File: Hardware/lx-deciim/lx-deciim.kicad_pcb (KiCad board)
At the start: 2 copper layers, 64.1 x 108 mm, 147 parts, among them IC1 AZ1117CH2-5.0TRG1, J1 AudioJack2_SwitchT, J10 AudioJack2_SwitchT, J11 AudioJack2_SwitchT, J12 AudioJack2_SwitchT, J13 AudioJack2_SwitchT, J14 AudioJack2_SwitchT, J15 AudioJack2_SwitchT, J16 AudioJack2_SwitchT, J17 Conn_01x10, J18 Conn_01x15_Pin, J19 Conn_01x15_Socket, J2 AudioJack2_SwitchT, J20 Conn_01x15_Pin, J21 Conn_01x15_Socket, J3 AudioJack2_SwitchT, J4 AudioJack2_SwitchT, J5 AudioJack2_SwitchT, J6 AudioJack2_SwitchT, J7 AudioJack2_SwitchT, J8 AudioJack2_SwitchT, J9 AudioJack2_SwitchT, U1 MCP6004, U2 MCP6001-OT, U3 MCP6004, U4 MCP6004, U5 TL074, U6 MCP6004

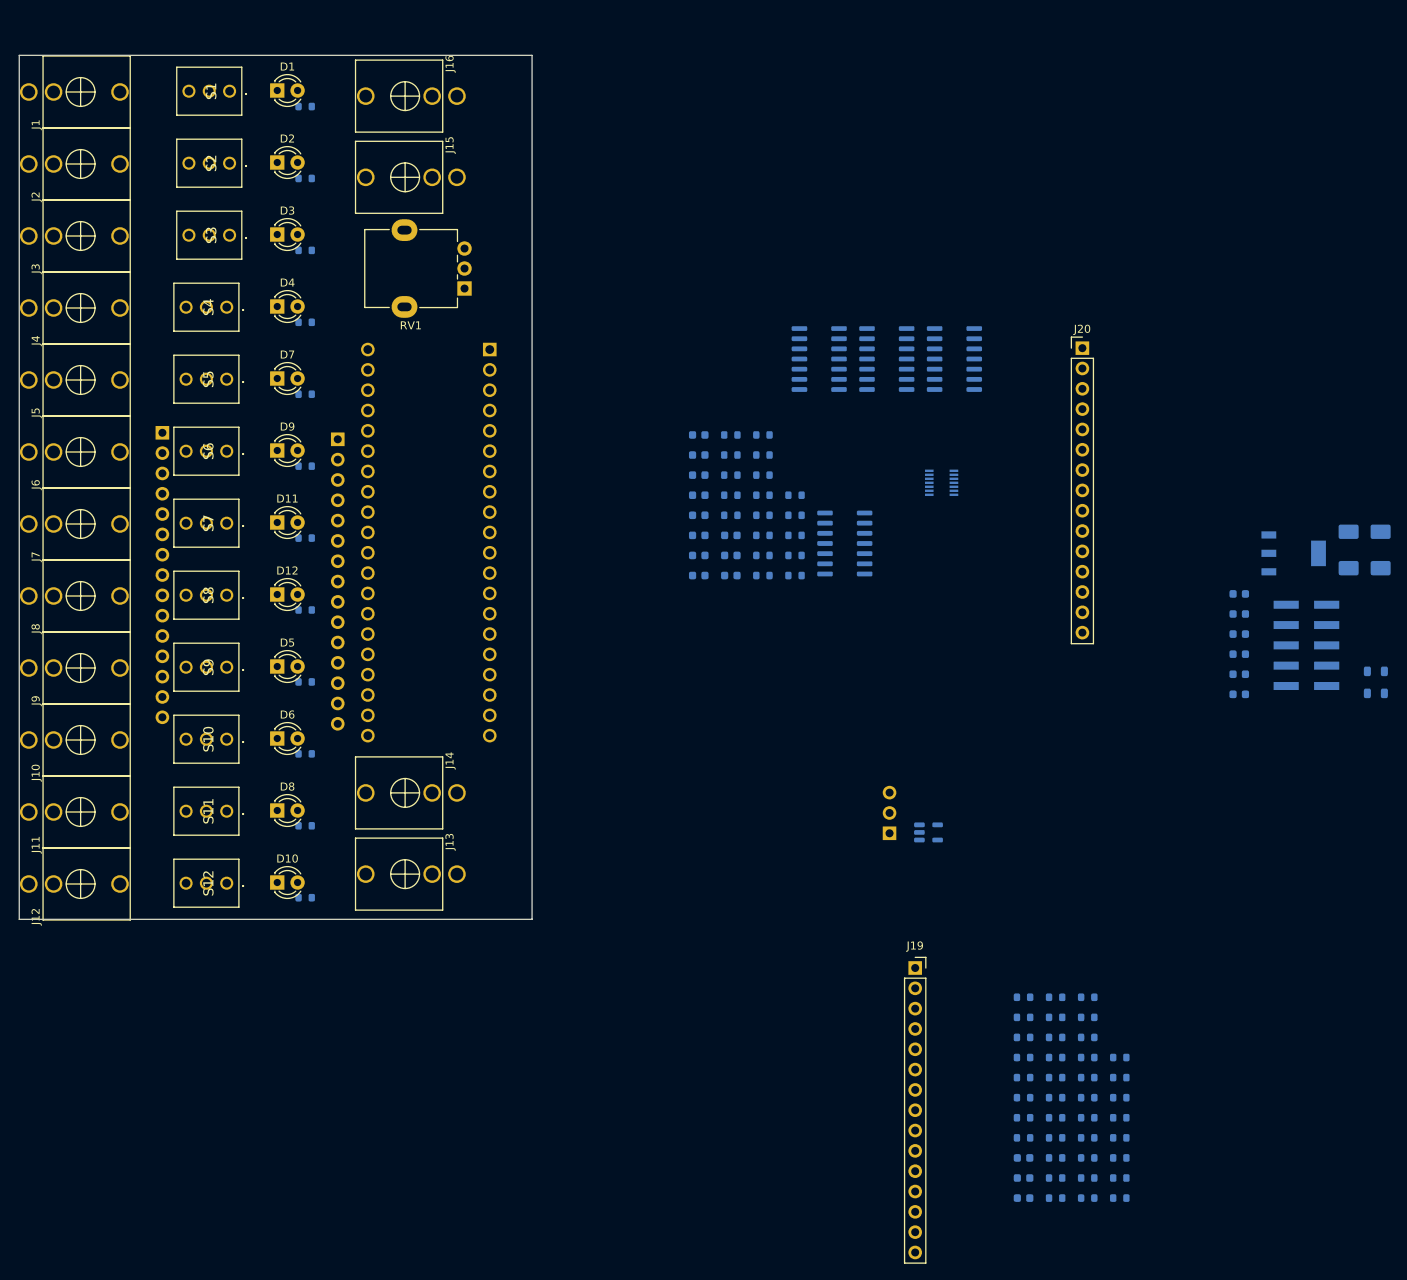
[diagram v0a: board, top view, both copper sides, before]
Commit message: feature: first draft routing
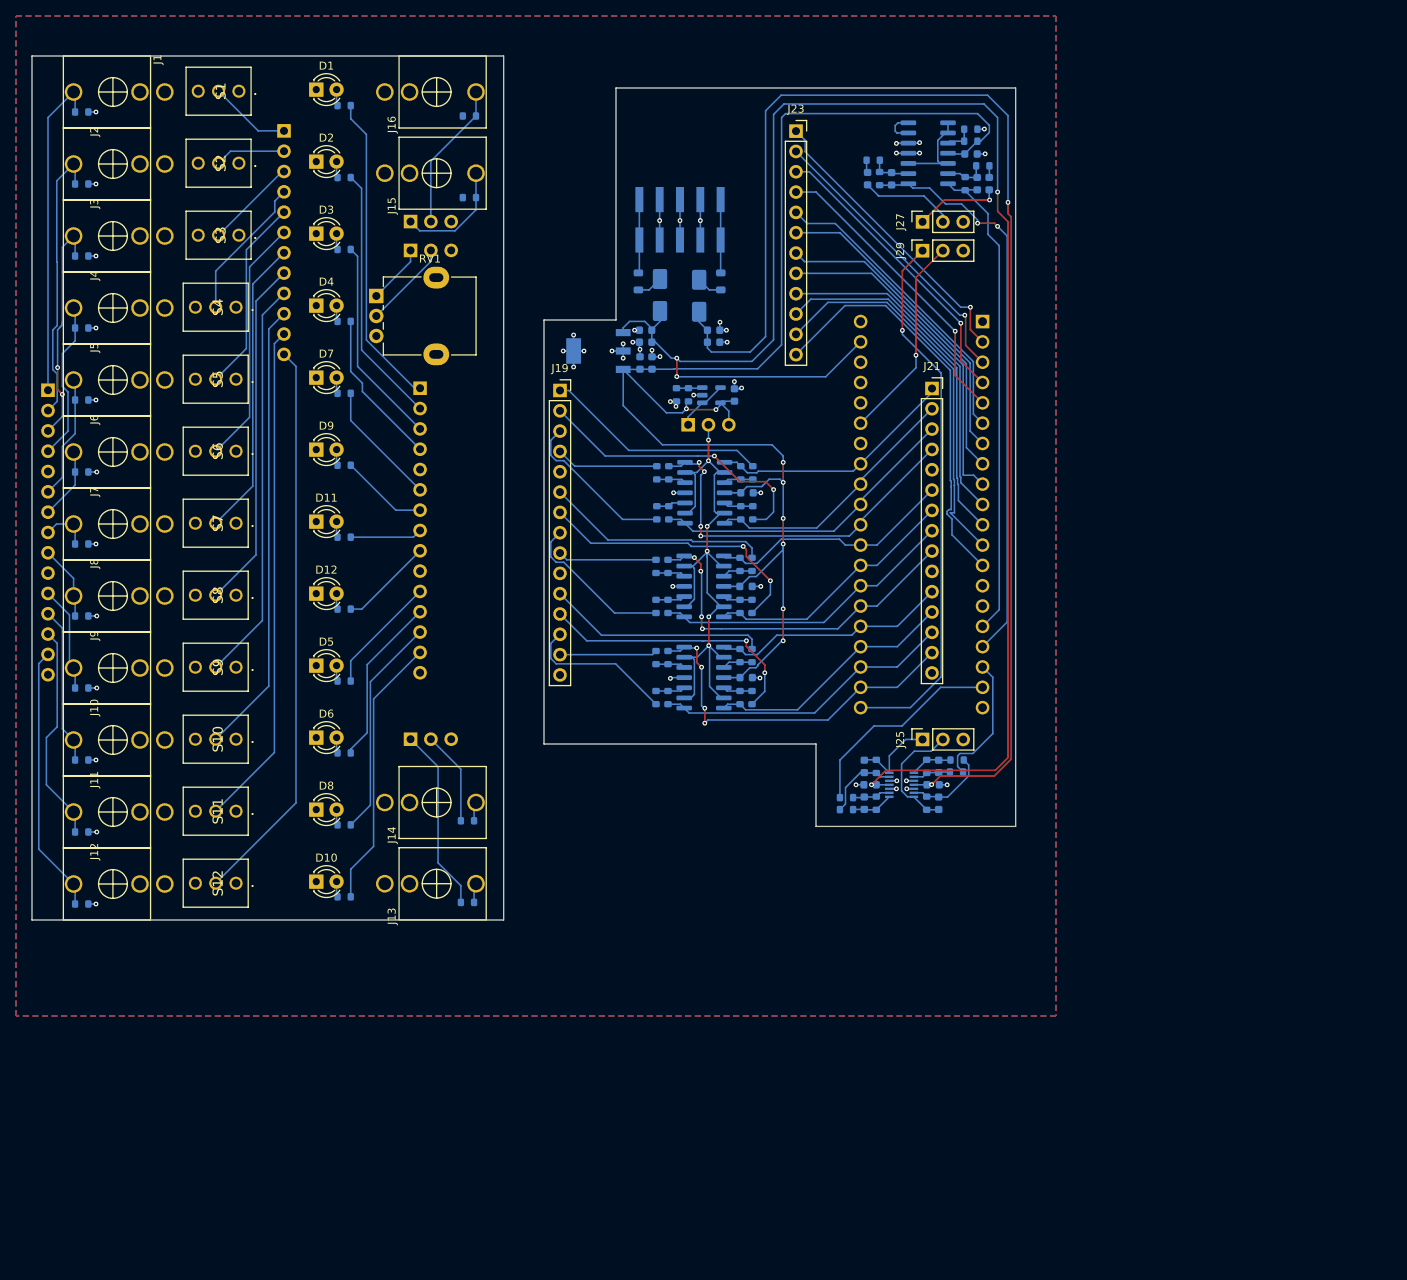
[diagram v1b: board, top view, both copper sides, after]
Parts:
- added C21: 100n, Capacitor_SMD:C_0603_1608Metric, B.Cu at (114.8, 72.4)
- added J22: Conn_01x12_Pin, Connector_PinHeader_2.54mm:PinHeader_1x12_P2.54mm_Vertical, B.Cu at (58.5, 39.4)
- added J23: Conn_01x12_Socket, Connector_PinSocket_2.54mm:PinSocket_1x12_P2.54mm_Vertical, F.Cu at (122.5, 39.4)
- added J24: Conn_01x03_Pin, Connector_PinHeader_2.54mm:PinHeader_1x03_P2.54mm_Vertical, B.Cu at (74.3, 115.4)
- added J25: Conn_01x03_Socket, Connector_PinSocket_2.54mm:PinSocket_1x03_P2.54mm_Vertical, F.Cu at (138.3, 115.4)
- added J26: Conn_01x03_Pin, Connector_PinHeader_2.54mm:PinHeader_1x03_P2.54mm_Vertical, B.Cu at (74.3, 50.7)
- added J27: Conn_01x03_Socket, Connector_PinSocket_2.54mm:PinSocket_1x03_P2.54mm_Vertical, F.Cu at (138.3, 50.7)
- added J28: Conn_01x03_Pin, Connector_PinHeader_2.54mm:PinHeader_1x03_P2.54mm_Vertical, B.Cu at (74.3, 54.3)
- added J29: Conn_01x03_Socket, Connector_PinSocket_2.54mm:PinSocket_1x03_P2.54mm_Vertical, F.Cu at (138.3, 54.3)
- J20: moved to B.Cu
- J21: moved to F.Cu
- moved R13 169.4 mm to (33.2, 55.0)
- moved R3 168.6 mm to (33.2, 37.0)
- moved R19 161.6 mm to (33.2, 64.0)
- moved R9 158.9 mm to (33.2, 46.0)
- moved R30 148.3 mm to (33.2, 73.0)
- moved R38 142.0 mm to (33.2, 82.0)
- moved R45 136.5 mm to (33.2, 91.0)
- moved R21 134.0 mm to (33.2, 109.0)
- moved R49 131.7 mm to (33.2, 100.0)
- moved R26 130.4 mm to (33.2, 118.0)
- moved R34 127.9 mm to (33.2, 127.0)
- moved R42 126.3 mm to (33.2, 136.0)
- moved FB1 105.6 mm to (102.8, 58.2), turned to -90 degrees
- moved R5 101.9 mm to (109.1, 72.3), turned to -90 degrees
- moved R7 100.2 mm to (107.6, 72.3), turned to 90 degrees
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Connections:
- A1 pad 10: /switches/sw_08 -> Net-(A1-SPI1_POCI)
- A1 pad 11: /switches/sw_09 -> Net-(A1-SPI1_PICO)
- A1 pad 12: /switches/sw_10 -> Net-(A1-I2C1_SCL)
- A1 pad 13: /switches/sw_11 -> Net-(A1-I2C1_SDA)
- A1 pad 2: /switches/sw_00 -> Net-(A1-SD_DATA_3)
- A1 pad 22: /triggers/trig_sig_00 -> trig_sig'_11
- A1 pad 23: /triggers/trig_sig_01 -> trig_sig'_10
- A1 pad 24: /triggers/trig_sig_02 -> trig_sig'_09
- A1 pad 25: /triggers/trig_sig_03 -> trig_sig'_08
- A1 pad 26: /triggers/trig_sig_04 -> trig_sig'_07
- A1 pad 27: /triggers/trig_sig_05 -> trig_sig'_06
- A1 pad 28: /triggers/trig_sig_06 -> trig_sig'_05
- A1 pad 29: /triggers/trig_sig_07 -> trig_sig'_04
- A1 pad 3: /switches/sw_01 -> Net-(A1-SD_DATA_2)
- A1 pad 30: /triggers/trig_sig_08 -> trig_sig'_03
- A1 pad 31: /triggers/trig_sig_09 -> trig_sig'_02
- A1 pad 32: /triggers/trig_sig_10 -> trig_sig'_01
- A1 pad 33: /triggers/trig_sig_11 -> trig_sig'_00
- A1 pad 4: /switches/sw_02 -> Net-(A1-SD_DATA_1)
- A1 pad 5: /switches/sw_03 -> Net-(A1-SD_DATA_0)
- A1 pad 6: /switches/sw_04 -> Net-(A1-SD_CMD)
- A1 pad 7: /switches/sw_05 -> Net-(A1-SD_CLK)
- A1 pad 8: /switches/sw_06 -> Net-(A1-SPI1_CS)
- A1 pad 9: /switches/sw_07 -> Net-(A1-SPI1_SCK)
- C11 pad 1: Net-(C11-Pad1) -> In'_R
- C14 pad 1: Net-(C14-Pad1) -> In'_L
- C5 pad 2: Net-(C5-Pad2) -> Out'_R
- C9 pad 2: Net-(C9-Pad2) -> Out'_L
- J15 pad T: Net-(C11-Pad1) -> In_R
- J16 pad T: Net-(C14-Pad1) -> In_L
- J20 pad 1: trig_sig'_00 -> trig_sig_00
- J20 pad 11: trig_sig'_08 -> trig_sig_08
- J20 pad 12: trig_sig'_09 -> trig_sig_09
- J20 pad 13: trig_sig'_10 -> trig_sig_10
- J20 pad 14: trig_sig'_11 -> trig_sig_11
- J20 pad 2: trig_sig'_01 -> trig_sig_01
- J20 pad 3: trig_sig'_02 -> trig_sig_02
- J20 pad 4: trig_sig'_03 -> trig_sig_03
- J20 pad 6: trig_sig'_04 -> trig_sig_04
- J20 pad 7: trig_sig'_05 -> trig_sig_05
- J20 pad 8: trig_sig'_06 -> trig_sig_06
- J20 pad 9: trig_sig'_07 -> trig_sig_07
- J21 pad 1: /triggers/trig_sig_00 -> trig_sig'_00
- J21 pad 11: /triggers/trig_sig_08 -> trig_sig'_08
- J21 pad 12: /triggers/trig_sig_09 -> trig_sig'_09
- J21 pad 13: /triggers/trig_sig_10 -> trig_sig'_10
- J21 pad 14: /triggers/trig_sig_11 -> trig_sig'_11
- J21 pad 2: /triggers/trig_sig_01 -> trig_sig'_01
- J21 pad 3: /triggers/trig_sig_02 -> trig_sig'_02
- J21 pad 4: /triggers/trig_sig_03 -> trig_sig'_03
- J21 pad 6: /triggers/trig_sig_04 -> trig_sig'_04
- J21 pad 7: /triggers/trig_sig_05 -> trig_sig'_05
- J21 pad 8: /triggers/trig_sig_06 -> trig_sig'_06
- J21 pad 9: /triggers/trig_sig_07 -> trig_sig'_07
- R10 pad 1: /triggers/trig_sig_01 -> trig_sig_01
- R13 pad 1: I'_02 -> I_02
- R14 pad 1: /triggers/trig_sig_02 -> trig_sig_02
- R19 pad 1: I'_03 -> I_03
- R20 pad 1: /triggers/trig_sig_03 -> trig_sig_03
- R21 pad 1: I'_08 -> I_08
- R22 pad 1: /triggers/trig_sig_08 -> trig_sig_08
- R26 pad 1: I'_09 -> I_09
- R27 pad 1: /triggers/trig_sig_09 -> trig_sig_09
- R3 pad 1: I'_00 -> I_00
- R30 pad 1: I'_04 -> I_04
- R31 pad 1: /triggers/trig_sig_04 -> trig_sig_04
- R34 pad 1: I'_10 -> I_10
- R35 pad 1: /triggers/trig_sig_10 -> trig_sig_10
- R38 pad 1: I'_05 -> I_05
- R39 pad 1: /triggers/trig_sig_05 -> trig_sig_05
- R4 pad 1: /triggers/trig_sig_00 -> trig_sig_00
- R42 pad 1: I'_11 -> I_11
- R43 pad 1: /triggers/trig_sig_11 -> trig_sig_11
- R45 pad 1: I'_06 -> I_06
- R46 pad 1: /triggers/trig_sig_06 -> trig_sig_06
- R49 pad 1: I'_07 -> I_07
- R50 pad 1: /triggers/trig_sig_07 -> trig_sig_07
- R52 pad 2: Net-(C5-Pad2) -> Out'_R
- R55 pad 2: Net-(C5-Pad2) -> Out_R
- R57 pad 2: Net-(C9-Pad2) -> Out'_L
- R60 pad 2: Net-(C9-Pad2) -> Out_L
- R64 pad 1: Net-(C11-Pad1) -> In_R
- R68 pad 1: Net-(C14-Pad1) -> In_L
- R9 pad 1: I'_01 -> I_01
- RV1 pad 1: +3V3 -> Net-(J28-Pin_1)
- RV1 pad 2: Net-(A1-SAI2_SCK) -> Net-(J28-Pin_2)
- U5 pad 14: Net-(C9-Pad2) -> Out'_L
- U5 pad 7: Net-(C5-Pad2) -> Out'_R
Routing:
- net +12V: track 0.00 -> 212.5 mm, vias 0 -> 4
- net +5V: track 0.00 -> 182.6 mm, vias 0 -> 8
- net -12V: track 0.00 -> 167.7 mm, vias 0 -> 2
- net trigger_comp_level: track 0.00 -> 81.2 mm, vias 0 -> 6
- net /audio_io/audio_in_L_daisy_level: track 0.00 -> 71.6 mm, vias 0 -> 2
- net /switches/sw_11: track 0.00 -> 70.9 mm
- net GND: track 0.00 -> 70.1 mm, vias 0 -> 53
- net +3V3: track 0.00 -> 68.0 mm, vias 0 -> 1
- net /switches/sw_10: track 0.00 -> 63.2 mm
- net /audio_io/audio_in_R_daisy_level: track 0.00 -> 61.1 mm
- net /switches/sw_09: track 0.00 -> 56.7 mm
- net Net-(A1-I2C1_SDA): track 0.00 -> 51.8 mm
- net /switches/sw_08: track 0.00 -> 50.3 mm
- net Net-(A1-I2C1_SCL): track 0.00 -> 49.0 mm
- net trig_sig'_03: track 0.00 -> 47.5 mm, vias 0 -> 4
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- added copper zone on B.Cu, net GND
- added copper zone on F.Cu, net GND
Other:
- board size 64.1 x 108 mm -> 123 x 108 mm

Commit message: feature: clean routing
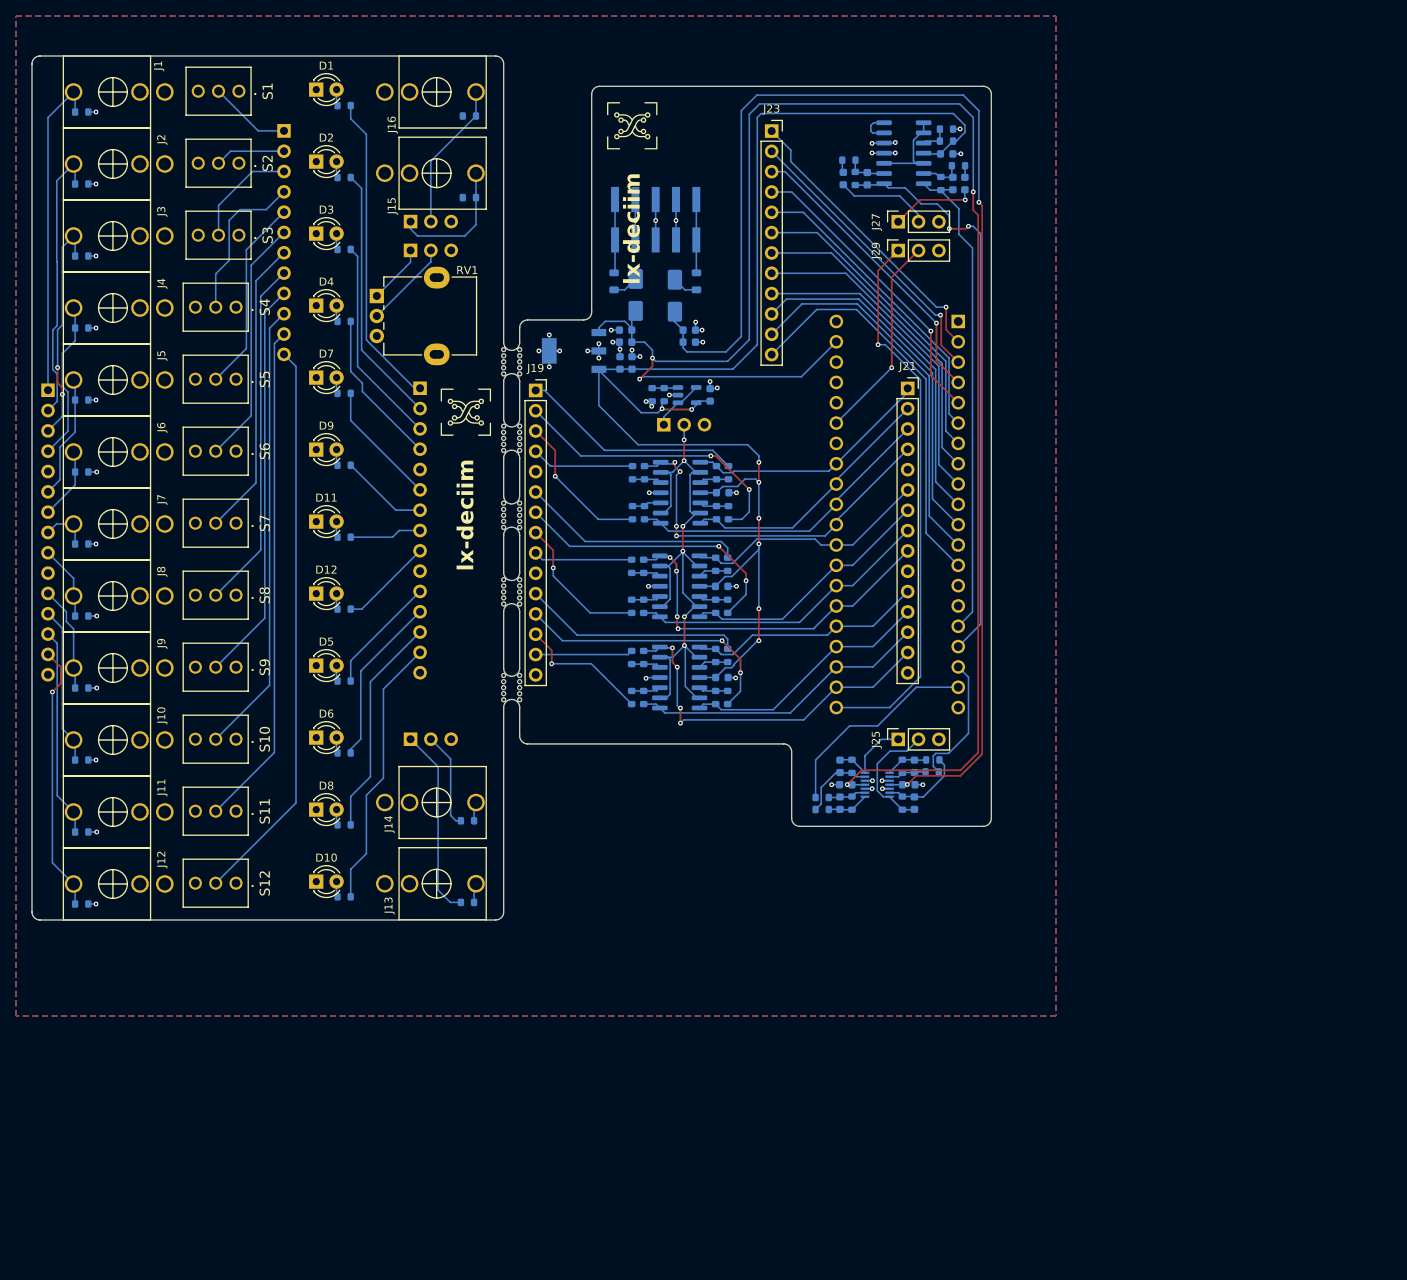
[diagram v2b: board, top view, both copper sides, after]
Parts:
- added ?: , , F.Cu at (88.0, 85.9)
- added ?: , , F.Cu at (86.0, 78.5)
- added ?: , , F.Cu at (88.0, 77.8)
- added ?: , , F.Cu at (86.0, 69.7)
- added ?: , , F.Cu at (86.0, 110.5)
- added ?: , , F.Cu at (88.0, 97.8)
- added ?: , , F.Cu at (88.0, 88.9)
- added ?: , , F.Cu at (86.0, 108.2)
- added ?: , , F.Cu at (88.0, 68.2)
- added ?: , , F.Cu at (88.0, 69.7)
- added ?: , , F.Cu at (88.0, 69.0)
- added ?: , , F.Cu at (88.0, 79.3)
- added ?: , , F.Cu at (86.0, 76.3)
- added ?: , , F.Cu at (88.0, 88.2)
- added ?: , , F.Cu at (88.0, 76.3)
- added ?: , , F.Cu at (88.0, 67.5)
- added ?: , , F.Cu at (86.0, 85.9)
- added ?: , , F.Cu at (88.0, 77.0)
- added ?: , , F.Cu at (86.0, 68.2)
- added ?: , , F.Cu at (86.0, 109.0)
- added ?: , , F.Cu at (88.0, 97.0)
- added ?: , , F.Cu at (86.0, 107.4)
- added ?: , , F.Cu at (88.0, 95.5)
- added ?: , , F.Cu at (86.0, 69.0)
- added ?: , , F.Cu at (88.0, 109.0)
- added ?: , , F.Cu at (86.0, 87.4)
- added ?: , , F.Cu at (88.0, 107.4)
- added ?: , , F.Cu at (88.0, 109.7)
- added ?: , , F.Cu at (88.0, 78.6)
- added ?: , , F.Cu at (86.0, 77.0)
- added ?: , , F.Cu at (86.0, 79.3)
- added ?: , , F.Cu at (86.0, 97.7)
- added ?: , , F.Cu at (88.0, 108.2)
- added ?: , , F.Cu at (86.0, 86.7)
- added ?: , , F.Cu at (86.0, 67.5)
- added ?: , , F.Cu at (88.0, 98.5)
- added ?: , , F.Cu at (86.0, 88.9)
- added ?: , , F.Cu at (86.0, 77.8)
- added ?: , , F.Cu at (88.0, 86.7)
- added ?: , , F.Cu at (86.0, 98.5)
- added ?: , , F.Cu at (88.0, 66.7)
- added ?: , , F.Cu at (86.0, 66.7)
- added ?: , , F.Cu at (86.0, 96.2)
- added ?: , , F.Cu at (88.0, 87.4)
- added ?: , , F.Cu at (88.0, 96.2)
- added ?: , , F.Cu at (86.0, 97.0)
- added ?: , , F.Cu at (86.0, 109.7)
- added ?: , , F.Cu at (88.0, 110.5)
- added ?: , , F.Cu at (86.0, 95.5)
- added ?: , , F.Cu at (86.0, 88.2)
- moved R51 3.04 mm to (129.5, 123.4)
- moved R52 3.04 mm to (129.5, 118.8)
- moved C19 3.04 mm to (109.2, 64.3)
- moved C2 3.04 mm to (113.2, 107.7)
- moved C20 3.04 mm to (109.2, 65.8)
- moved C21 3.04 mm to (111.8, 72.4)
- moved C4 3.04 mm to (128.0, 123.4)
- moved D13 3.04 mm to (102.5, 59.9)
- moved D14 3.04 mm to (107.4, 60.0)
- moved J17 3.04 mm to (105.0, 50.5)
- moved J19 3.04 mm to (90.0, 71.8)
- moved J23 3.04 mm to (119.5, 39.4)
- moved R16 3.04 mm to (112.5, 104.9)
- moved R18 3.04 mm to (114.0, 104.9)
- moved R23 3.04 mm to (112.5, 110.2)
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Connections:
- JP1 pad 3: +5V -> GND
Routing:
- net +5V: track 182.6 -> 179.4 mm
- net I'_10: track 19.0 -> 16.6 mm, vias 0 -> 1
- net /switches/sw_02: track 11.5 -> 13.7 mm
- net In_R: track 14.3 -> 16.5 mm
- net /switches/sw_03: track 18.0 -> 19.9 mm
- net +12V: track 212.5 -> 214.3 mm
- net trigger_comp_level: track 81.2 -> 79.5 mm
- net Net-(A1-I2C1_SDA): track 51.8 -> 50.2 mm
- net I'_06: track 19.6 -> 18.0 mm, vias 0 -> 1
- net I'_02: track 20.1 -> 18.6 mm, vias 0 -> 1
- net Net-(A1-I2C1_SCL): track 49.0 -> 47.6 mm
- net -12V: track 167.7 -> 166.5 mm
- net +3V3: track 68.0 -> 69.2 mm
- net I_10: track 27.3 -> 26.1 mm
- net I_02: track 29.7 -> 28.8 mm
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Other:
- board size 123 x 108 mm -> 119.9 x 108 mm
- board text added: "-12V red line"
- board text added: "0V"
- board text added: "2.5V"
- board text added: "Build by the SN"
- board text added: "Comparator ref"
- board text added: "GND"
- board text added: "lx-deciim"
- board text added: "lx-deciim v1.0.0 12.06.2025 logic-board Lucas Bonvin"
- board text added: "lx-deciim v1.0.0 12.06.2025 main-board Lucas Bonvin"
